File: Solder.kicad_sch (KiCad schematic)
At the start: 13 parts, among them Q1 NPN, Q2 NPN, Q3 NPN, Q4 NPN, SW1 SW_Push, SW2 SW_Push

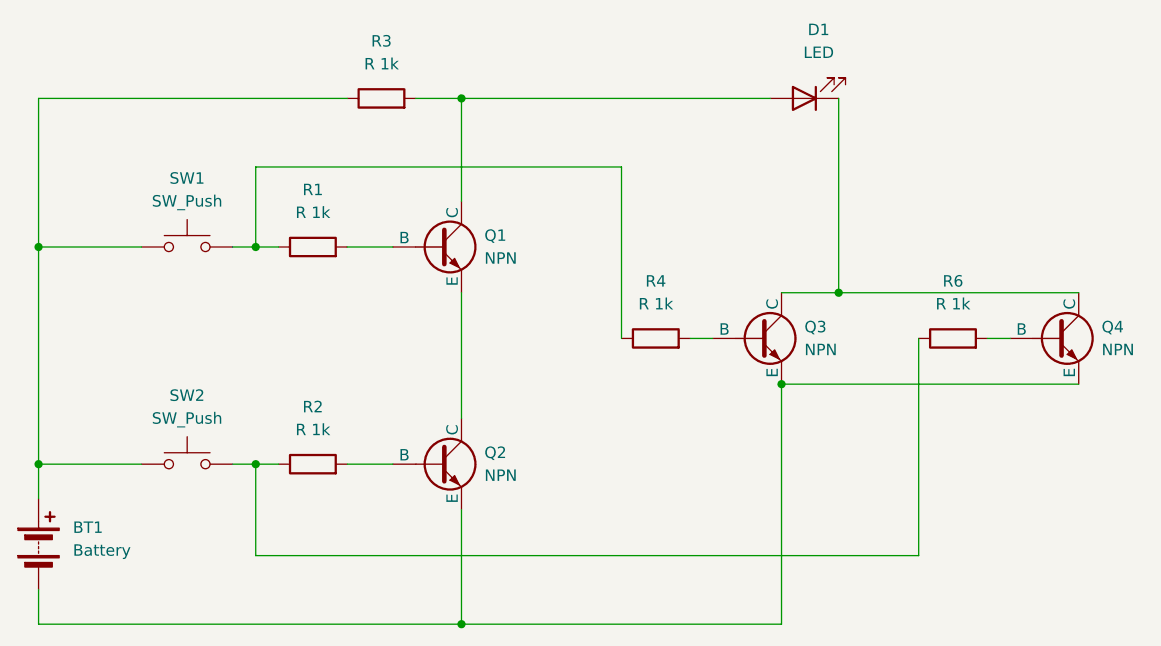
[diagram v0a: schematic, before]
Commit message: added logos to the back
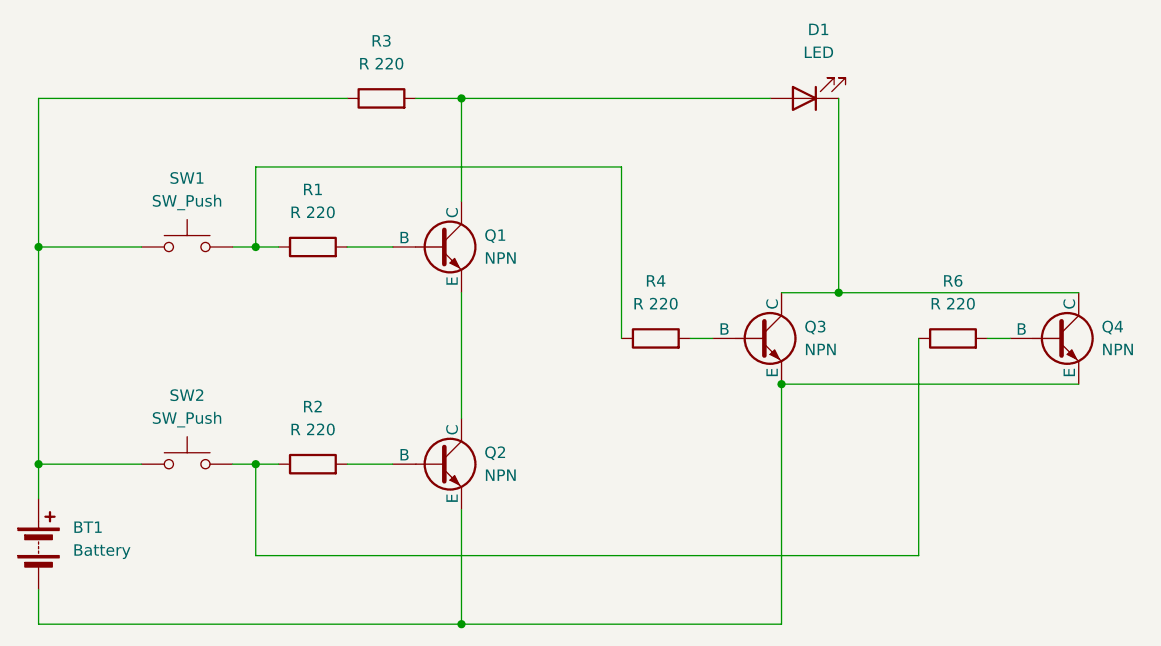
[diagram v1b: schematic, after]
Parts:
- R1, R2, R3, R4, R6: value R 1k -> R 220
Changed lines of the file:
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@@
 			)
 		)
-		(property "Value" "R 1k"
+		(property "Value" "R 220"
 			(at 133.35 99.06 90)
 			(effects
@@
 			)
 		)
-		(property "Value" "R 1k"
+		(property "Value" "R 220"
 			(at 95.25 113.03 90)
 			(effects
@@
 			)
 		)
-		(property "Value" "R 1k"
+		(property "Value" "R 220"
 			(at 102.87 72.39 90)
 			(effects
@@
 			)
 		)
-		(property "Value" "R 1k"
+		(property "Value" "R 220"
 			(at 166.37 99.06 90)
 			(effects
@@
 			)
 		)
-		(property "Value" "R 1k"
+		(property "Value" "R 220"
 			(at 95.25 88.9 90)
 			(effects
